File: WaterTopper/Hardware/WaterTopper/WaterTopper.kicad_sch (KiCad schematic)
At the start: 26 parts, among them J1 TYPE-C-31-M-12, J2 Barrel_Jack_Switch, J3 Conn_01x07, J4 Conn_01x04, J5 Conn_01x04, J6 Conn_01x04, J7 Conn_01x04, J8 Screw_Terminal_01x02, J9 Screw_Terminal_01x02, U1 AP2112K-3.3, U2 ESP32-S3-MINI-1-N8, U3 DRV8881PRHRT

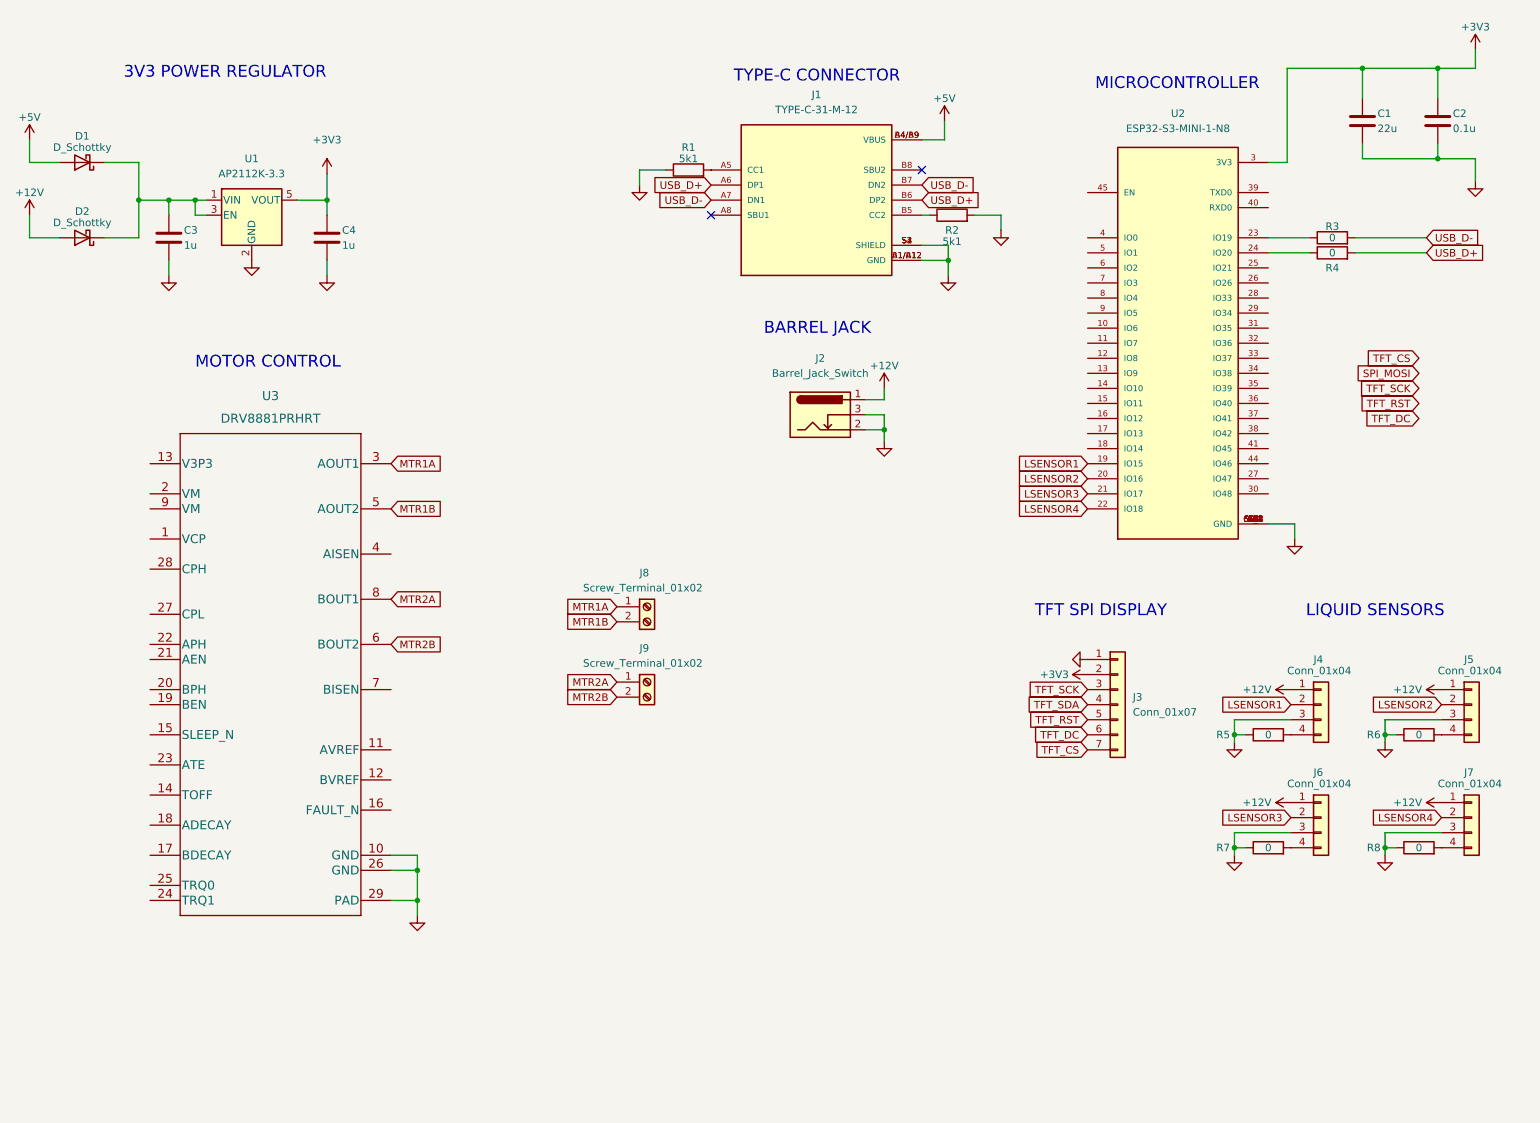
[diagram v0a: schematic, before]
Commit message: Finished WaterTopper schematic
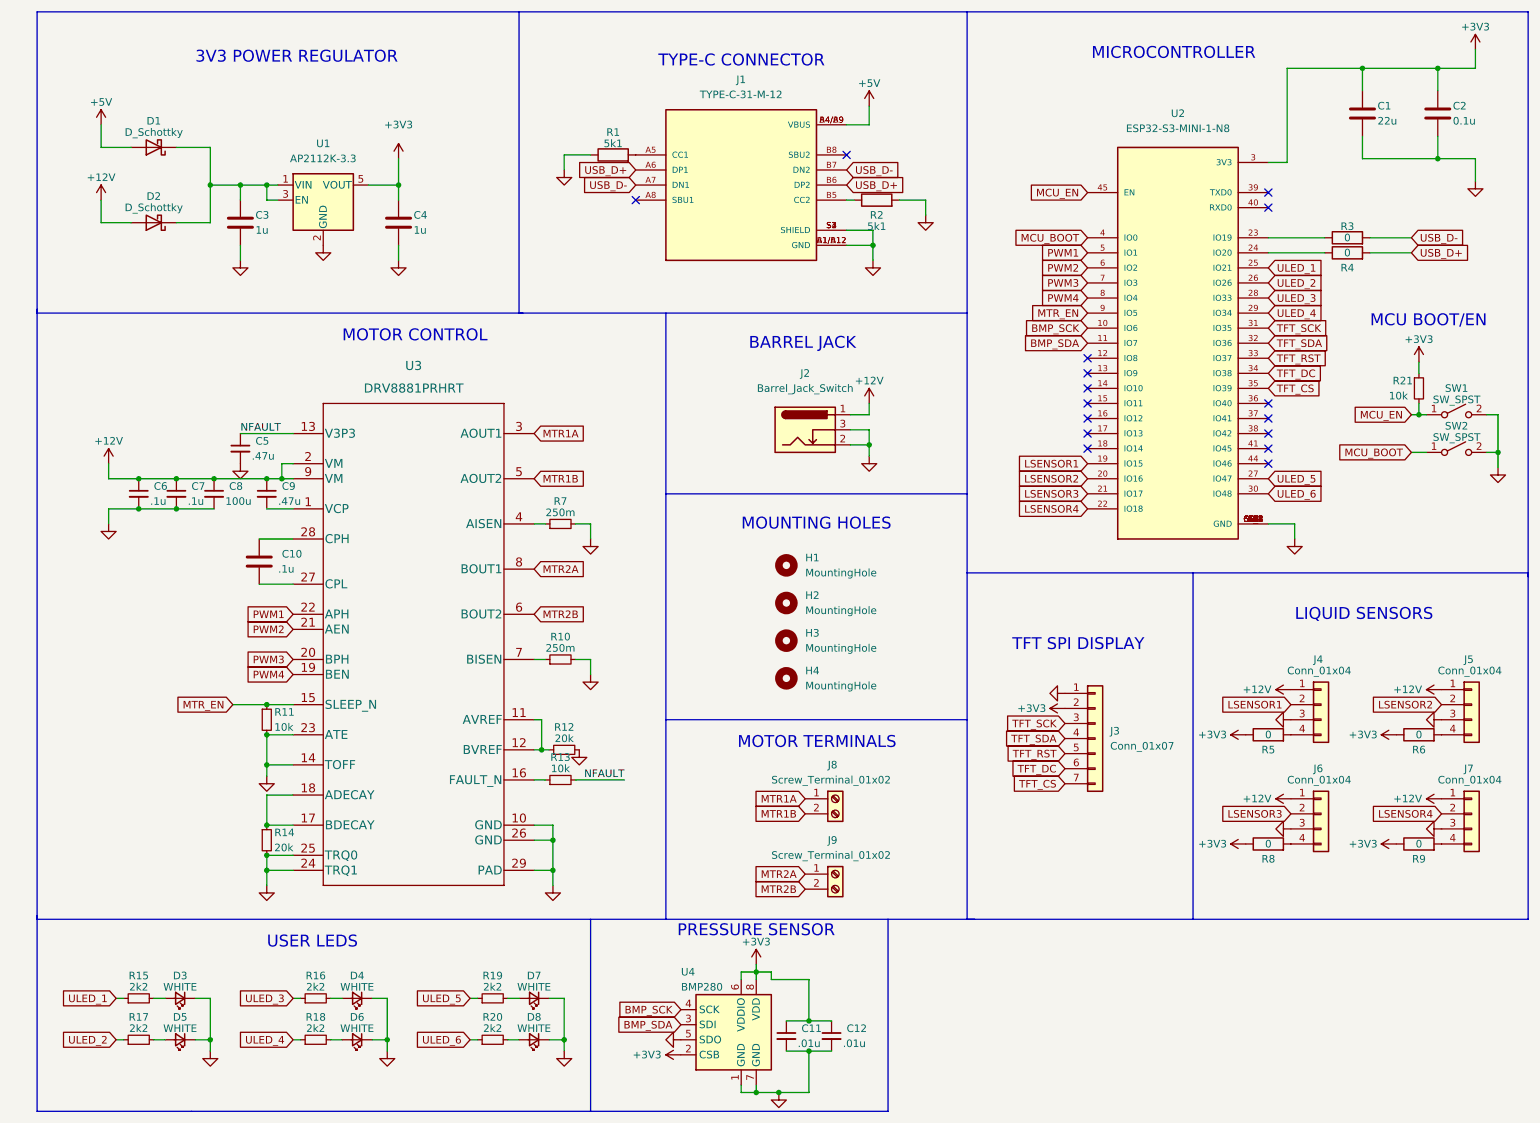
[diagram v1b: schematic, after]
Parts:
- removed R7: 0, Capacitor_SMD:C_01005_0402Metric, symbol Device:R
- added C10: .1u, symbol Device:C
- added C11, C12: .01u, symbol Device:C_Small
- added C5, C9: .47u, symbol Device:C_Small
- added C6, C7: .1u, symbol Device:C_Small
- added C8: 100u, symbol Device:C_Small
- added D3, D4, D5, D6, D7, D8: WHITE, symbol Device:LED_Small
- added H1, H2, H3, H4: MountingHole, MountingHole:MountingHole_2.7mm_M2.5, symbol Mechanical:MountingHole
- added R10, R7: 250m, symbol Device:R_Small
- added R11, R13, R21: 10k, symbol Device:R_Small
- added R12, R14: 20k, symbol Device:R_Small
- added R15, R16, R17, R18, R19, R20: 2k2, symbol Device:R_Small
- added R9: 0, Capacitor_SMD:C_01005_0402Metric, symbol Device:R
- added SW1, SW2: SW_SPST, symbol Switch:SW_SPST
- added U4: BMP280, Package_LGA:Bosch_LGA-8_2x2.5mm_P0.65mm_ClockwisePinNumbering, symbol Sensor_Pressure:BMP280
- D1, D2: footprint (none) -> Diode_SMD:D_SMA
- J2: footprint (none) -> Connector_BarrelJack:BarrelJack_Wuerth_6941xx301002
- J3: footprint (none) -> Connector_PinHeader_2.00mm:PinHeader_1x07_P2.00mm_Vertical
- J4: footprint (none) -> Connector_JST:JST_XH_S4B-XH-A-1_1x04_P2.50mm_Horizontal
- J5, J6, J7: footprint (none) -> Connector_JST:JST_XH_S4B-XH-A_1x04_P2.50mm_Horizontal
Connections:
- net +12V: now also U3.2 (VM), U3.9 (VM), C6.1, C7.1, C8.1, C9.1
- net +3V3: now also R5.1, R6.1, R8.1, C11.1, C12.1, R21.1, R9.1, U4.2 (CSB), U4.6 (VDDIO), U4.8 (VDD)
- net GND: now also U3.14 (TOFF), U3.23 (ATE), U3.24 (TRQ1), U3.25 (TRQ0), C11.2, C12.2, C5.2, C6.2, C7.2, C8.2, D3.1 (K), D4.1 (K), D5.1 (K), D6.1 (K), D7.1 (K), D8.1 (K), R10.2, R11.2, R12.2, R14.2, R7.2, SW1.2 (B), SW2.2 (B), U4.1 (GND), U4.5 (SDO), U4.7 (GND); no longer R5.1, R6.1, R8.1
- net TFT_CS: now also U2.35 (IO39)
- net TFT_DC: now also U2.34 (IO38)
- net TFT_RST: now also U2.33 (IO37)
- net TFT_SCK: now also U2.31 (IO35)
- net TFT_SDA: now also U2.32 (IO36)
- net at J6.4 (Pin_4): now also R8.2
- net at U3.1 (VCP): now also C9.2
- net at U3.11 (AVREF): now also U3.12 (BVREF), R12.1
- net NFAULT: now reaches U3.13 (V3P3)
- net NFAULT: now also C5.1, R13.2
- net MTR_EN: now reaches U3.15 (SLEEP_N)
- net MTR_EN: now also U2.9 (IO5), R11.1
- net at U3.16 (FAULT_N): now also R13.1
- net at U3.17 (BDECAY): now also U3.18 (ADECAY), R14.1
- net PWM4: now reaches U3.19 (BEN)
- net PWM4: now also U2.8 (IO4)
- net PWM3: now reaches U3.20 (BPH)
- net PWM3: now also U2.7 (IO3)
- net PWM2: now reaches U3.21 (AEN)
- net PWM2: now also U2.6 (IO2)
- net PWM1: now reaches U3.22 (APH)
- net PWM1: now also U2.5 (IO1)
- net at U3.27 (CPL): now also C10.2
- net at U3.28 (CPH): now also C10.1
- net at U3.4 (AISEN): now also R7.1
- net at U3.7 (BISEN): now also R10.1
- net at J7.4 (Pin_4): now also R9.2; no longer R8.2
- net BMP_SCK: now reaches U2.10 (IO6)
- net BMP_SCK: now also U4.4 (SCK)
- net BMP_SDA: now reaches U2.11 (IO7)
- net BMP_SDA: now also U4.3 (SDI)
- net ULED_1: now reaches U2.25 (IO21)
- net ULED_1: now also R15.1
- net ULED_2: now reaches U2.26 (IO26)
- net ULED_2: now also R17.1
- net ULED_5: now reaches U2.27 (IO47)
- net ULED_5: now also R19.1
- net ULED_3: now reaches U2.28 (IO33)
- net ULED_3: now also R16.1
- net ULED_4: now reaches U2.29 (IO34)
- net ULED_4: now also R18.1
- net ULED_6: now reaches U2.30 (IO48)
- net ULED_6: now also R20.1
- net MCU_BOOT: now reaches U2.4 (IO0)
- net MCU_BOOT: now also SW2.1 (A)
- net MCU_EN: now reaches U2.45 (EN)
- net MCU_EN: now also R21.2, SW1.1 (A)
- new net: D5.2 (A), R17.2
- new net: D8.2 (A), R20.2
- new net: D6.2 (A), R18.2
- new net: D7.2 (A), R19.2
- new net: D3.2 (A), R15.2
- new net: D4.2 (A), R16.2
- no-connect marks 2 -> 16
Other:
- note added: "MCU BOOT/EN"
- note added: "MOTOR TERMINALS"
- note added: "MOUNTING HOLES"
- note added: "PRESSURE SENSOR"
- note added: "USER LEDS"
- company: (none) -> Byron Chan
- title: (none) -> WaterTopper
- moved on the sheet: C1, C2, C3, C4, D1, D2, J1, J2, J3, J8, J9, R1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

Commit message: Updated pcb design
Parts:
- C10, C11, C12, C5, C6, C7, C8, C9: footprint (none) -> Capacitor_SMD:C_01005_0402Metric
- D3, D4, D5, D6, D7, D8: footprint (none) -> LED_SMD:LED_0201_0603Metric
- J4: footprint Connector_JST:JST_XH_S4B-XH-A-1_1x04_P2.50mm_Horizontal -> Connector_JST:JST_PH_B4B-PH-K_1x04_P2.00mm_Vertical
- J5, J6, J7: footprint Connector_JST:JST_XH_S4B-XH-A_1x04_P2.50mm_Horizontal -> Connector_JST:JST_PH_B4B-PH-K_1x04_P2.00mm_Vertical
- R10, R11, R12, R13, R14, R15, R16, R17, R18, R19, R20, R21, R7: footprint (none) -> Resistor_SMD:R_01005_0402Metric
- SW1, SW2: footprint (none) -> Button_Switch_SMD:SW_SPST_PTS810
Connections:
- net ULED_3: now also U2.27 (IO47); no longer U2.28 (IO33)
- net ULED_4: now also U2.28 (IO33); no longer U2.29 (IO34)
- net ULED_5: now also U2.29 (IO34); no longer U2.27 (IO47)

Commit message: Updated pcb + 4 layer
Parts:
- C1: footprint Capacitor_SMD:C_0201_0603Metric -> Capacitor_SMD:C_0805_2012Metric
- C10, C11, C12, C2, C5, C6, C7, C9: footprint Capacitor_SMD:C_01005_0402Metric -> Capacitor_SMD:C_0603_1608Metric
- C3, C4: footprint Capacitor_SMD:C_01005_0402Metric -> Capacitor_SMD:C_0805_2012Metric
- C8: footprint Capacitor_SMD:C_01005_0402Metric -> Capacitor_SMD:C_Elec_6.3x5.8
- D3, D4, D5, D6, D7, D8: footprint LED_SMD:LED_0201_0603Metric -> LED_SMD:LED_0603_1608Metric
- H1, H2, H3, H4: footprint MountingHole:MountingHole_2.7mm_M2.5 -> MountingHole:MountingHole_3.2mm_M3
- R1, R2, R3, R4, R5, R6, R8, R9: footprint Capacitor_SMD:C_01005_0402Metric -> Resistor_SMD:R_0603_1608Metric
- R10, R11, R12, R13, R14, R15, R16, R17, R18, R19, R20, R21, R7: footprint Resistor_SMD:R_01005_0402Metric -> Resistor_SMD:R_0603_1608Metric

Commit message: Completed pcb v0.1
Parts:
- J1: MANUFACTURER HRO Electronics Co., Ltd. -> HRO Electronics; MAXIMUM_PACKAGE_HEIGHT 3.26 mm -> 3.31mm; PARTREV 2020.12.08 -> A; SNAPEDA_PN TYPE-C-31-M-12 -> (none)
- renumbered D7 to D1, D8 to D2, D4 to D3, D6 to D4, D3 to D5, D5 to D6, D1 to D7, D2 to D8
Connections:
- net +5V: now also J1.A4B9 (VBUS), J1.B4A9 (VBUS); no longer J1.A4/B9 (VBUS), J1.B4/A9 (VBUS)
- net BMP_SCK: now also U2.21 (IO17); no longer U2.10 (IO6)
- net BMP_SDA: now also U2.22 (IO18); no longer U2.11 (IO7)
- net GND: now also J1.A1B12 (GND), J1.B1A12 (GND); no longer J1.A1/B12 (GND), J1.B1/A12 (GND)
- net LSENSOR1: now also U2.17 (IO13); no longer U2.19 (IO15)
- net LSENSOR2: now also U2.18 (IO14); no longer U2.20 (IO16)
- net LSENSOR3: now also U2.19 (IO15); no longer U2.21 (IO17)
- net LSENSOR4: now also U2.20 (IO16); no longer U2.22 (IO18)
- net MTR2A: now also J9.2 (Pin_2); no longer J9.1 (Pin_1)
- net MTR2B: now also J9.1 (Pin_1); no longer J9.2 (Pin_2)
- net MTR_EN: now also U2.38 (IO42); no longer U2.9 (IO5)
- net PWM1: now also U2.34 (IO38); no longer U2.5 (IO1)
- net PWM2: now also U2.35 (IO39); no longer U2.6 (IO2)
- net PWM3: now also U2.36 (IO40); no longer U2.7 (IO3)
- net PWM4: now also U2.37 (IO41); no longer U2.8 (IO4)
- net TFT_CS: now also U2.12 (IO8); no longer U2.35 (IO39)
- net TFT_DC: now also U2.13 (IO9); no longer U2.34 (IO38)
- net TFT_RST: now also U2.14 (IO10); no longer U2.33 (IO37)
- net TFT_SCK: now also U2.16 (IO12); no longer U2.31 (IO35)
- net TFT_SDA: now also U2.15 (IO11); no longer U2.32 (IO36)
- net ULED_1: now also R19.1, U2.5 (IO1); no longer R15.1, U2.25 (IO21)
- net ULED_2: now also R20.1, U2.6 (IO2); no longer R17.1, U2.26 (IO26)
- net ULED_3: now also U2.8 (IO4); no longer U2.27 (IO47)
- net ULED_4: now also U2.9 (IO5); no longer U2.28 (IO33)
- net ULED_5: now also R15.1, U2.10 (IO6); no longer R19.1, U2.29 (IO34)
- net ULED_6: now also R17.1, U2.11 (IO7); no longer R20.1, U2.30 (IO48)
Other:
- moved on the sheet: D1, D2, D5, D6, R15, R17, R19, R20
